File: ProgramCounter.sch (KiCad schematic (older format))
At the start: 6 parts, among them U29 74LS245, U30 74LS245, U31 74LS161, U32 74LS161, U33 74LS161, U34 74LS161

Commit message: Added NAND GATES in ALU
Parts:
- renumbered U29 to U13, U30 to U14, U31 to U15, U32 to U16, U33 to U17, U34 to U18
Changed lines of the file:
@@
 $Descr A3 16535 11693
 encoding utf-8
-Sheet 9 20
+Sheet 9 21
 Title ""
 Date ""
@@
 AR Path="/603B766D/5F6D5FCC" Ref="#PWR?"  Part="1"
 AR Path="/5F74778C/5F6D5FCC" Ref="#PWR?"  Part="1"
-AR Path="/5F6ACD14/5F6D5FCC" Ref="#PWR091"  Part="1"
-F 0 "#PWR091" H 4750 4200 50  0001 C CNN
+AR Path="/5F6ACD14/5F6D5FCC" Ref="#PWR072"  Part="1"
+F 0 "#PWR072" H 4750 4200 50  0001 C CNN
 F 1 "GND" H 4755 4277 50  0000 C CNN
 F 2 "" H 4750 4450 50  0001 C CNN
@@
 AR Path="/603B766D/5F6D5FE4" Ref="#PWR?"  Part="1"
 AR Path="/5F74778C/5F6D5FE4" Ref="#PWR?"  Part="1"
-AR Path="/5F6ACD14/5F6D5FE4" Ref="#PWR087"  Part="1"
-F 0 "#PWR087" H 3150 3400 50  0001 C CNN
+AR Path="/5F6ACD14/5F6D5FE4" Ref="#PWR068"  Part="1"
+F 0 "#PWR068" H 3150 3400 50  0001 C CNN
 F 1 "GND" H 3155 3477 50  0000 C CNN
 F 2 "" H 3150 3650 50  0001 C CNN
@@
 AR Path="/603B766D/5F6D5FF6" Ref="#PWR?"  Part="1"
 AR Path="/5F74778C/5F6D5FF6" Ref="#PWR?"  Part="1"
-AR Path="/5F6ACD14/5F6D5FF6" Ref="#PWR089"  Part="1"
-F 0 "#PWR089" H 3150 4300 50  0001 C CNN
+AR Path="/5F6ACD14/5F6D5FF6" Ref="#PWR070"  Part="1"
+F 0 "#PWR070" H 3150 4300 50  0001 C CNN
 F 1 "+5V" H 3165 4623 50  0000 C CNN
 F 2 "" H 3150 4450 50  0001 C CNN
@@
 AR Path="/603B766D/5F6D6094" Ref="U?"  Part="1"
 AR Path="/5F74778C/5F6D6094" Ref="U?"  Part="1"
-AR Path="/5F6ACD14/5F6D6094" Ref="U29"  Part="1"
-F 0 "U29" V 2396 2806 50  0000 R CNN
+AR Path="/5F6ACD14/5F6D6094" Ref="U13"  Part="1"
+F 0 "U13" V 2396 2806 50  0000 R CNN
 F 1 "74LS245" V 2305 2806 50  0000 R CNN
 F 2 "Package_DIP:DIP-20_W7.62mm" H 2350 3650 50  0001 C CNN
@@
 AR Path="/603B766D/5F6D60A0" Ref="#PWR?"  Part="1"
 AR Path="/5F74778C/5F6D60A0" Ref="#PWR?"  Part="1"
-AR Path="/5F6ACD14/5F6D60A0" Ref="#PWR092"  Part="1"
-F 0 "#PWR092" H 4750 4200 50  0001 C CNN
+AR Path="/5F6ACD14/5F6D60A0" Ref="#PWR073"  Part="1"
+F 0 "#PWR073" H 4750 4200 50  0001 C CNN
 F 1 "GND" H 4755 4277 50  0000 C CNN
 F 2 "" H 4750 4450 50  0001 C CNN
@@
 AR Path="/603B766D/5F6D60B8" Ref="#PWR?"  Part="1"
 AR Path="/5F74778C/5F6D60B8" Ref="#PWR?"  Part="1"
-AR Path="/5F6ACD14/5F6D60B8" Ref="#PWR088"  Part="1"
-F 0 "#PWR088" H 3150 3400 50  0001 C CNN
+AR Path="/5F6ACD14/5F6D60B8" Ref="#PWR069"  Part="1"
+F 0 "#PWR069" H 3150 3400 50  0001 C CNN
 F 1 "GND" H 3155 3477 50  0000 C CNN
 F 2 "" H 3150 3650 50  0001 C CNN
@@
 AR Path="/603B766D/5F6D60C4" Ref="#PWR?"  Part="1"
 AR Path="/5F74778C/5F6D60C4" Ref="#PWR?"  Part="1"
-AR Path="/5F6ACD14/5F6D60C4" Ref="#PWR085"  Part="1"
-F 0 "#PWR085" H 1550 3500 50  0001 C CNN
+AR Path="/5F6ACD14/5F6D60C4" Ref="#PWR066"  Part="1"
+F 0 "#PWR066" H 1550 3500 50  0001 C CNN
 F 1 "+5V" H 1565 3823 50  0000 C CNN
 F 2 "" H 1550 3650 50  0001 C CNN
@@
 AR Path="/603B766D/5F6D60D0" Ref="#PWR?"  Part="1"
 AR Path="/5F74778C/5F6D60D0" Ref="#PWR?"  Part="1"
-AR Path="/5F6ACD14/5F6D60D0" Ref="#PWR090"  Part="1"
-F 0 "#PWR090" H 3150 4300 50  0001 C CNN
+AR Path="/5F6ACD14/5F6D60D0" Ref="#PWR071"  Part="1"
+F 0 "#PWR071" H 3150 4300 50  0001 C CNN
 F 1 "+5V" H 3165 4623 50  0000 C CNN
 F 2 "" H 3150 4450 50  0001 C CNN
@@
 AR Path="/603B766D/5F6D6117" Ref="U?"  Part="1"
 AR Path="/5F74778C/5F6D6117" Ref="U?"  Part="1"
-AR Path="/5F6ACD14/5F6D6117" Ref="U30"  Part="1"
-F 0 "U30" V 3996 3606 50  0000 R CNN
+AR Path="/5F6ACD14/5F6D6117" Ref="U14"  Part="1"
+F 0 "U14" V 3996 3606 50  0000 R CNN
 F 1 "74LS245" V 3905 3606 50  0000 R CNN
 F 2 "Package_DIP:DIP-20_W7.62mm" H 3950 4450 50  0001 C CNN
@@
 AR Path="/603B766D/5F6D6186" Ref="#PWR?"  Part="1"
 AR Path="/5F74778C/5F6D6186" Ref="#PWR?"  Part="1"
-AR Path="/5F6ACD14/5F6D6186" Ref="#PWR086"  Part="1"
-F 0 "#PWR086" H 1550 3500 50  0001 C CNN
+AR Path="/5F6ACD14/5F6D6186" Ref="#PWR067"  Part="1"
+F 0 "#PWR067" H 1550 3500 50  0001 C CNN
 F 1 "+5V" H 1565 3823 50  0000 C CNN
 F 2 "" H 1550 3650 50  0001 C CNN
@@
 	1550 4650 1550 3650
 $Comp
-L 16bitCpu-rescue:74LS161-74xx U31
+L 16bitCpu-rescue:74LS161-74xx U?
 U 1 1 5F779E04
 P 6100 4450
-AR Path="/5F779E04" Ref="U31"  Part="1"
-AR Path="/5F6ACD14/5F779E04" Ref="U31"  Part="1"
-F 0 "U31" V 6054 5294 50  0000 L CNN
+AR Path="/5F779E04" Ref="U?"  Part="1"
+AR Path="/5F6ACD14/5F779E04" Ref="U15"  Part="1"
+F 0 "U15" V 6054 5294 50  0000 L CNN
 F 1 "74LS161" V 6145 5294 50  0000 L CNN
 F 2 "Package_DIP:DIP-16_W7.62mm" H 6100 4450 50  0001 C CNN
@@
 $EndComp
 $Comp
-L 16bitCpu-rescue:74LS161-74xx U33
+L 16bitCpu-rescue:74LS161-74xx U?
 U 1 1 5F77F8AA
 P 9900 4450
-AR Path="/5F77F8AA" Ref="U33"  Part="1"
-AR Path="/5F6ACD14/5F77F8AA" Ref="U33"  Part="1"
-F 0 "U33" V 9854 5294 50  0000 L CNN
+AR Path="/5F77F8AA" Ref="U?"  Part="1"
+AR Path="/5F6ACD14/5F77F8AA" Ref="U17"  Part="1"
+F 0 "U17" V 9854 5294 50  0000 L CNN
 F 1 "74LS161" V 9945 5294 50  0000 L CNN
 F 2 "Package_DIP:DIP-16_W7.62mm" H 9900 4450 50  0001 C CNN
@@
 $EndComp
 $Comp
-L 16bitCpu-rescue:74LS161-74xx U34
+L 16bitCpu-rescue:74LS161-74xx U?
 U 1 1 5F780CA7
 P 11750 4450
-AR Path="/5F780CA7" Ref="U34"  Part="1"
-AR Path="/5F6ACD14/5F780CA7" Ref="U34"  Part="1"
-F 0 "U34" V 11704 5294 50  0000 L CNN
+AR Path="/5F780CA7" Ref="U?"  Part="1"
+AR Path="/5F6ACD14/5F780CA7" Ref="U18"  Part="1"
+F 0 "U18" V 11704 5294 50  0000 L CNN
 F 1 "74LS161" V 11795 5294 50  0000 L CNN
 F 2 "Package_DIP:DIP-16_W7.62mm" H 11750 4450 50  0001 C CNN
@@
 	8050 4950 8050 5200
 $Comp
-L 16bitCpu-rescue:74LS161-74xx U32
+L 16bitCpu-rescue:74LS161-74xx U?
 U 1 1 5F77E072
 P 8050 4450
-AR Path="/5F77E072" Ref="U32"  Part="1"
-AR Path="/5F6ACD14/5F77E072" Ref="U32"  Part="1"
-F 0 "U32" V 8004 5294 50  0000 L CNN
+AR Path="/5F77E072" Ref="U?"  Part="1"
+AR Path="/5F6ACD14/5F77E072" Ref="U16"  Part="1"
+F 0 "U16" V 8004 5294 50  0000 L CNN
 F 1 "74LS161" V 8095 5294 50  0000 L CNN
 F 2 "Package_DIP:DIP-16_W7.62mm" H 8050 4450 50  0001 C CNN
@@
 	6900 4450 6900 4250
 $Comp
-L 16bitCpu-rescue:+5V-power #PWR094
+L 16bitCpu-rescue:+5V-power #PWR?
 U 1 1 5F9A8E46
 P 6900 4250
-AR Path="/5F9A8E46" Ref="#PWR094"  Part="1"
-AR Path="/5F6ACD14/5F9A8E46" Ref="#PWR094"  Part="1"
-F 0 "#PWR094" H 6900 4100 50  0001 C CNN
+AR Path="/5F9A8E46" Ref="#PWR?"  Part="1"
+AR Path="/5F6ACD14/5F9A8E46" Ref="#PWR075"  Part="1"
+F 0 "#PWR075" H 6900 4100 50  0001 C CNN
 F 1 "+5V" H 6915 4423 50  0000 C CNN
 F 2 "" H 6900 4250 50  0001 C CNN
@@
 $EndComp
 $Comp
-L 16bitCpu-rescue:+5V-power #PWR096
+L 16bitCpu-rescue:+5V-power #PWR?
 U 1 1 5F9B1DDA
 P 8850 4400
-AR Path="/5F9B1DDA" Ref="#PWR096"  Part="1"
-AR Path="/5F6ACD14/5F9B1DDA" Ref="#PWR096"  Part="1"
-F 0 "#PWR096" H 8850 4250 50  0001 C CNN
+AR Path="/5F9B1DDA" Ref="#PWR?"  Part="1"
+AR Path="/5F6ACD14/5F9B1DDA" Ref="#PWR077"  Part="1"
+F 0 "#PWR077" H 8850 4250 50  0001 C CNN
 F 1 "+5V" H 8865 4573 50  0000 C CNN
 F 2 "" H 8850 4400 50  0001 C CNN
@@
 	8850 4400 8850 4450
 $Comp
-L 16bitCpu-rescue:+5V-power #PWR098
+L 16bitCpu-rescue:+5V-power #PWR?
 U 1 1 5F9BCAE2
 P 10700 4450
-AR Path="/5F9BCAE2" Ref="#PWR098"  Part="1"
-AR Path="/5F6ACD14/5F9BCAE2" Ref="#PWR098"  Part="1"
-F 0 "#PWR098" H 10700 4300 50  0001 C CNN
+AR Path="/5F9BCAE2" Ref="#PWR?"  Part="1"
+AR Path="/5F6ACD14/5F9BCAE2" Ref="#PWR079"  Part="1"
+F 0 "#PWR079" H 10700 4300 50  0001 C CNN
 F 1 "+5V" H 10715 4623 50  0000 C CNN
 F 2 "" H 10700 4450 50  0001 C CNN
@@
 $EndComp
 $Comp
-L 16bitCpu-rescue:+5V-power #PWR0100
+L 16bitCpu-rescue:+5V-power #PWR?
 U 1 1 5F9BD87F
 P 12550 4450
-AR Path="/5F9BD87F" Ref="#PWR0100"  Part="1"
-AR Path="/5F6ACD14/5F9BD87F" Ref="#PWR0100"  Part="1"
-F 0 "#PWR0100" H 12550 4300 50  0001 C CNN
+AR Path="/5F9BD87F" Ref="#PWR?"  Part="1"
+AR Path="/5F6ACD14/5F9BD87F" Ref="#PWR081"  Part="1"
+F 0 "#PWR081" H 12550 4300 50  0001 C CNN
 F 1 "+5V" H 12565 4623 50  0000 C CNN
 F 2 "" H 12550 4450 50  0001 C CNN
@@
 $EndComp
 $Comp
-L 16bitCpu-rescue:GND-power #PWR093
+L 16bitCpu-rescue:GND-power #PWR?
 U 1 1 5F9BEDE2
 P 5300 4450
-AR Path="/5F9BEDE2" Ref="#PWR093"  Part="1"
-AR Path="/5F6ACD14/5F9BEDE2" Ref="#PWR093"  Part="1"
-F 0 "#PWR093" H 5300 4200 50  0001 C CNN
+AR Path="/5F9BEDE2" Ref="#PWR?"  Part="1"
+AR Path="/5F6ACD14/5F9BEDE2" Ref="#PWR074"  Part="1"
+F 0 "#PWR074" H 5300 4200 50  0001 C CNN
 F 1 "GND" H 5305 4277 50  0000 C CNN
 F 2 "" H 5300 4450 50  0001 C CNN
@@
 $EndComp
 $Comp
-L 16bitCpu-rescue:GND-power #PWR095
+L 16bitCpu-rescue:GND-power #PWR?
 U 1 1 5F9C426E
 P 7250 4450
-AR Path="/5F9C426E" Ref="#PWR095"  Part="1"
-AR Path="/5F6ACD14/5F9C426E" Ref="#PWR095"  Part="1"
-F 0 "#PWR095" H 7250 4200 50  0001 C CNN
+AR Path="/5F9C426E" Ref="#PWR?"  Part="1"
+AR Path="/5F6ACD14/5F9C426E" Ref="#PWR076"  Part="1"
+F 0 "#PWR076" H 7250 4200 50  0001 C CNN
 F 1 "GND" H 7255 4277 50  0000 C CNN
 F 2 "" H 7250 4450 50  0001 C CNN
@@
 $EndComp
 $Comp
-L 16bitCpu-rescue:GND-power #PWR097
+L 16bitCpu-rescue:GND-power #PWR?
 U 1 1 5F9CE333
 P 9100 4450
-AR Path="/5F9CE333" Ref="#PWR097"  Part="1"
-AR Path="/5F6ACD14/5F9CE333" Ref="#PWR097"  Part="1"
-F 0 "#PWR097" H 9100 4200 50  0001 C CNN
+AR Path="/5F9CE333" Ref="#PWR?"  Part="1"
+AR Path="/5F6ACD14/5F9CE333" Ref="#PWR078"  Part="1"
+F 0 "#PWR078" H 9100 4200 50  0001 C CNN
 F 1 "GND" H 9105 4277 50  0000 C CNN
 F 2 "" H 9100 4450 50  0001 C CNN
@@
 $EndComp
 $Comp
-L 16bitCpu-rescue:GND-power #PWR099
+L 16bitCpu-rescue:GND-power #PWR?
 U 1 1 5F9D8AA1
 P 10950 4450
-AR Path="/5F9D8AA1" Ref="#PWR099"  Part="1"
-AR Path="/5F6ACD14/5F9D8AA1" Ref="#PWR099"  Part="1"
-F 0 "#PWR099" H 10950 4200 50  0001 C CNN
+AR Path="/5F9D8AA1" Ref="#PWR?"  Part="1"
+AR Path="/5F6ACD14/5F9D8AA1" Ref="#PWR080"  Part="1"
+F 0 "#PWR080" H 10950 4200 50  0001 C CNN
 F 1 "GND" H 10955 4277 50  0000 C CNN
 F 2 "" H 10950 4450 50  0001 C CNN

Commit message: fixed more errors
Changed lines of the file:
@@
-$EndComp
-$Comp
-L 16bitCpu-rescue:GND-power #PWR?
-U 1 1 5F6D5FE4
-P 3150 3650
-AR Path="/5F6D5FE4" Ref="#PWR?"  Part="1"
-AR Path="/5F67C726/5F6D5FE4" Ref="#PWR?"  Part="1"
-AR Path="/5F70885A/5F6D5FE4" Ref="#PWR?"  Part="1"
-AR Path="/5F733C5E/5F6D5FE4" Ref="#PWR?"  Part="1"
-AR Path="/602D4838/5F6D5FE4" Ref="#PWR?"  Part="1"
-AR Path="/603B00C8/5F6D5FE4" Ref="#PWR?"  Part="1"
-AR Path="/603B766D/5F6D5FE4" Ref="#PWR?"  Part="1"
-AR Path="/5F74778C/5F6D5FE4" Ref="#PWR?"  Part="1"
-AR Path="/5F6ACD14/5F6D5FE4" Ref="#PWR068"  Part="1"
-F 0 "#PWR068" H 3150 3400 50  0001 C CNN
-F 1 "GND" H 3155 3477 50  0000 C CNN
-F 2 "" H 3150 3650 50  0001 C CNN
-F 3 "" H 3150 3650 50  0001 C CNN
-	1    3150 3650
-	1    0    0    -1
 $EndComp
 $Comp

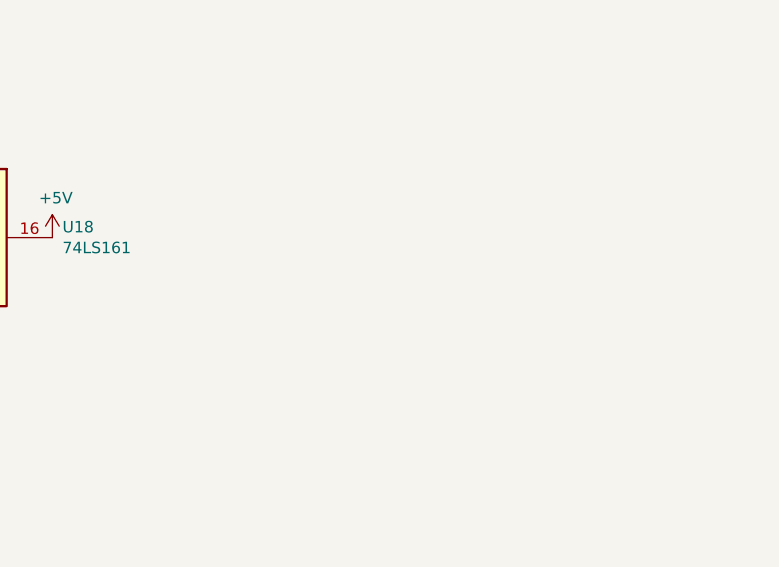
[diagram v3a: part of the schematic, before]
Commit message: added power caps
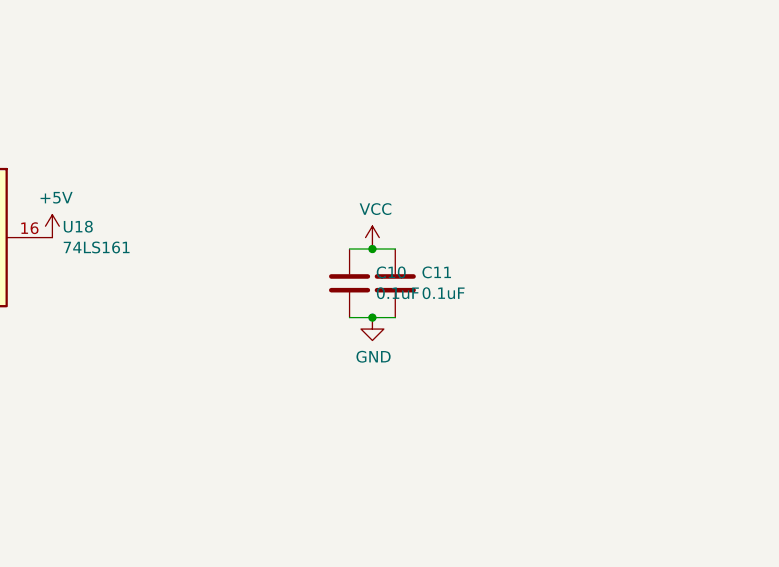
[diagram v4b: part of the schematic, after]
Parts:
- added C10, C11: 0.1uF, Capacitor_THT:CP_Axial_L10.0mm_D4.5mm_P15.00mm_Horizontal, symbol Device:C
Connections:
- net labels added: VCC
- wire segments 239 -> 243
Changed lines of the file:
@@
 Wire Wire Line
 	6100 6000 4150 6000
+$Comp
+L 16bitCpu-rescue:VCC-power #PWR?
+U 1 1 5FB038A7
+P 13950 4500
+AR Path="/5FB038A7" Ref="#PWR?"  Part="1"
+AR Path="/5F6ACD14/5FB038A7" Ref="#PWR0263"  Part="1"
+F 0 "#PWR0263" H 13950 4350 50  0001 C CNN
+F 1 "VCC" H 13965 4673 50  0000 C CNN
+F 2 "" H 13950 4500 50  0001 C CNN
+F 3 "" H 13950 4500 50  0001 C CNN
+	1    13950 4500
+	1    0    0    -1
+$EndComp
+$Comp
+L 16bitCpu-rescue:GND-power #PWR?
+U 1 1 5FB038AD
+P 13950 4800
+AR Path="/5FB038AD" Ref="#PWR?"  Part="1"
+AR Path="/5F75E433/5FB038AD" Ref="#PWR?"  Part="1"
+AR Path="/5F6ACD14/5FB038AD" Ref="#PWR0264"  Part="1"
+F 0 "#PWR0264" H 13950 4550 50  0001 C CNN
+F 1 "GND" H 13955 4627 50  0000 C CNN
+F 2 "" H 13950 4800 50  0001 C CNN
+F 3 "" H 13950 4800 50  0001 C CNN
+	1    13950 4800
+	1    0    0    -1
+$EndComp
+Wire Wire Line
+	13950 4500 14050 4500
+Wire Wire Line
+	14050 4800 13950 4800
+$Comp
+L Device:C C?
+U 1 1 5FB038B5
+P 13850 4650
+AR Path="/5F75E433/5FB038B5" Ref="C?"  Part="1"
+AR Path="/5F6ACD14/5FB038B5" Ref="C10"  Part="1"
+F 0 "C10" H 13965 4696 50  0000 L CNN
+F 1 "0.1uF" H 13965 4605 50  0000 L CNN
+F 2 "Capacitor_THT:CP_Axial_L10.0mm_D4.5mm_P15.00mm_Horizontal" H 13888 4500 50  0001 C CNN
+F 3 "" H 13850 4650 50  0001 C CNN
+	1    13850 4650
+	1    0    0    -1
+$EndComp
+Wire Wire Line
+	13950 4500 13850 4500
+Connection ~ 13950 4500
+Wire Wire Line
+	13850 4800 13950 4800
+Connection ~ 13950 4800
+$Comp
+L Device:C C?
+U 1 1 5FB038BF
+P 14050 4650
+AR Path="/5F75E433/5FB038BF" Ref="C?"  Part="1"
+AR Path="/5F6ACD14/5FB038BF" Ref="C11"  Part="1"
+F 0 "C11" H 14165 4696 50  0000 L CNN
+F 1 "0.1uF" H 14165 4605 50  0000 L CNN
+F 2 "Capacitor_THT:CP_Axial_L10.0mm_D4.5mm_P15.00mm_Horizontal" H 14088 4500 50  0001 C CNN
+F 3 "" H 14050 4650 50  0001 C CNN
+	1    14050 4650
+	1    0    0    -1
+$EndComp
 $EndSCHEMATC
